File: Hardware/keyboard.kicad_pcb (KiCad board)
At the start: 2 copper layers, 228.8 x 97.4 mm, 57 parts, among them M1 Tab, M10 O, M11 P, M12 Backspace, M13 Esc, M14 A, M15 S, M16 D, M17 F, M18 G, M19 H, M2 Q, M20 J, M21 K, M22 L, M23 ;, M24 ', M25 Shift, M26 Z, M27 X, M28 C, M29 V, M3 W, M30 B, M31 N, M32 M, M33 ,, M34 ., M35 /, M36 Enter, M37 Blnk, M38 Ctrl, M39 Alt, M4 E, M40 Super, M41 Down, M42 Space, M43 Up, M44 L_Ar, M45 D_Ar, M46 U_Ar, M47 R_Ar, M5 R, M6 T, M7 Y, M8 U, M9 I, U1 ROW_1, U2 ROW_2, U3 ROW_3

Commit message: Update
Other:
- outline, holes or cut-outs redrawn
- board text removed: ""Write bussy on it" -Suyash"
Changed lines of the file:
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@@
   (general
     (thickness 1.6)
-    (drawings 7)
+    (drawings 4)
     (tracks 377)
     (zones 0)
@@
     (add_net /SDA_)
     (add_net GND)
-    (add_net "Net-(C1-Pad10)")
-    (add_net "Net-(C1-Pad11)")
-    (add_net "Net-(C1-Pad12)")
-    (add_net "Net-(C1-Pad2)")
-    (add_net "Net-(C1-Pad8)")
-    (add_net "Net-(C1-Pad9)")
-    (add_net "Net-(U1-Pad19)")
-    (add_net "Net-(U2-Pad19)")
-    (add_net "Net-(U2-Pad3)")
-    (add_net "Net-(U3-Pad19)")
   )
   (module Resistor_THT:R_Axial_DIN0204_L3.6mm_D1.6mm_P7.62mm_Horizontal (layer F.Cu)
@@
       (effects (font (size 1 1) (thickness 0.15)))
     )
-    (fp_text user %R (at 3.81 0) (layer F.Fab)
-      (effects (font (size 0.72 0.72) (thickness 0.108)))
-    )
     (fp_line (start 2.01 -0.8) (end 2.01 0.8) (layer F.Fab) (width 0.1))
     (fp_line (start 2.01 0.8) (end 5.61 0.8) (layer F.Fab) (width 0.1))
@@
     (fp_line (start 8.57 1.05) (end 8.57 -1.05) (layer F.CrtYd) (width 0.05))
     (fp_line (start 8.57 -1.05) (end -0.95 -1.05) (layer F.CrtYd) (width 0.05))
+    (fp_text user %R (at 3.81 0) (layer F.Fab)
+      (effects (font (size 0.72 0.72) (thickness 0.108)))
+    )
     (pad 2 thru_hole oval (at 7.62 0 180) (size 1.4 1.4) (drill 0.7) (layers *.Cu *.Mask)
       (net 34 /SCL_))
@@
       (effects (font (size 1 1) (thickness 0.15)))
     )
-    (fp_text user %R (at 3.81 0) (layer F.Fab)
-      (effects (font (size 0.72 0.72) (thickness 0.108)))
-    )
     (fp_line (start 2.01 -0.8) (end 2.01 0.8) (layer F.Fab) (width 0.1))
     (fp_line (start 2.01 0.8) (end 5.61 0.8) (layer F.Fab) (width 0.1))
@@
     (fp_line (start 8.57 1.05) (end 8.57 -1.05) (layer F.CrtYd) (width 0.05))
     (fp_line (start 8.57 -1.05) (end -0.95 -1.05) (layer F.CrtYd) (width 0.05))
+    (fp_text user %R (at 3.81 0) (layer F.Fab)
+      (effects (font (size 0.72 0.72) (thickness 0.108)))
+    )
     (pad 2 thru_hole oval (at 7.62 0 180) (size 1.4 1.4) (drill 0.7) (layers *.Cu *.Mask)
       (net 2 +5V))
@@
   (gr_line (start 101.346 186.182) (end 101.346 88.7476) (layer Edge.Cuts) (width 0.05))
   (gr_line (start 330.1492 186.182) (end 101.346 186.182) (layer Edge.Cuts) (width 0.05))
-  (gr_line (start 101.346 88.7476) (end 327.8632 88.7476) (layer Edge.Cuts) (width 0.05))
-  (gr_line (start 101.346 88.7476) (end 329.9968 88.7476) (layer Edge.Cuts) (width 0.05))
   (gr_line (start 330.1492 88.7476) (end 101.346 88.7476) (layer Edge.Cuts) (width 0.05))
   (gr_line (start 330.1492 186.182) (end 330.1492 88.7476) (layer Edge.Cuts) (width 0.05))
-  (gr_text "\"Write bussy on it\" -Suyash" (at 210.185 146.685) (layer B.SilkS)
-    (effects (font (size 7 7) (thickness 1)) (justify mirror))
-  )
+  (segment (start 293.330908 91.31874) (end 293.72687 91.714702) (width 0.25) (layer F.Cu) (net 0))
   (segment (start 119.47525 108.1564) (end 113.6809 113.95075) (width 0.25) (layer F.Cu) (net 1))
   (segment (start 119.47525 103.345011) (end 119.47525 108.1564) (width 0.25) (layer F.Cu) (net 1))
@@
   (segment (start 251.215901 157.216099) (end 265.132302 171.1325) (width 0.25) (layer F.Cu) (net 33))
   (segment (start 113.325559 91.714702) (end 109.31525 95.725011) (width 0.254) (layer F.Cu) (net 34))
-  (segment (start 293.330908 91.31874) (end 293.72687 91.714702) (width 0.25) (layer F.Cu) (net 0))
   (segment (start 113.325559 91.714702) (end 113.721521 91.31874) (width 0.25) (layer F.Cu) (net 34))
   (segment (start 172.322083 95.725011) (end 176.53 91.517094) (width 0.25) (layer B.Cu) (net 34))

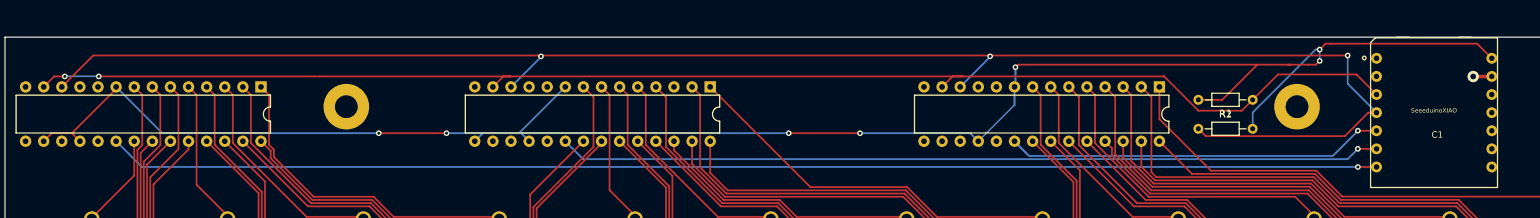
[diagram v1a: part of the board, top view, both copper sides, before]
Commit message: Swapped SDA and SCL pins.
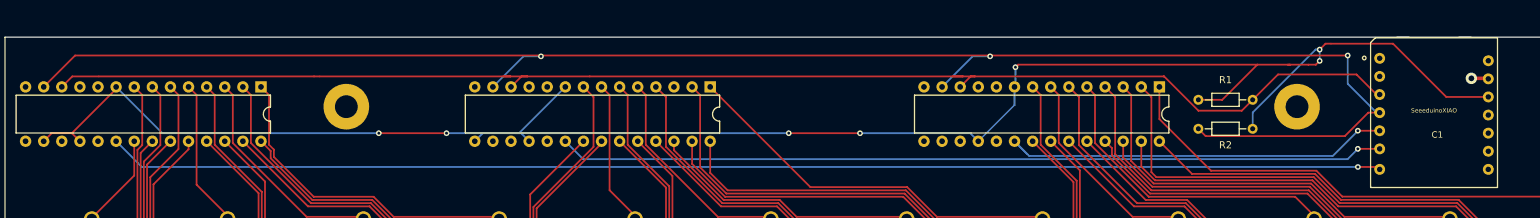
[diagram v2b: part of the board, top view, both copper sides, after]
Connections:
- C1 pad 12: (no net) -> +3V3
- C1 pad 14: +5V -> (no net)
- C1 pad 3: /SDA_ -> /SCL_
- C1 pad 4: /SCL_ -> /SDA_
- R1 pad 1: /SDA_ -> /SCL_
- R1 pad 2: +5V -> +3V3
- R2 pad 1: +5V -> +3V3
- R2 pad 2: /SCL_ -> /SDA_
- U1 pad 18: +5V -> +3V3
- U1 pad 9: +5V -> +3V3
- U2 pad 15: +5V -> +3V3
- U2 pad 18: +5V -> +3V3
- U2 pad 9: +5V -> +3V3
- U3 pad 16: +5V -> +3V3
- U3 pad 18: +5V -> +3V3
- U3 pad 9: +5V -> +3V3
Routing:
- net +3V3: track 0.00 -> 262.9 mm, vias 0 -> 7
- net +5V: track 261.2 -> 0.00 mm, vias 7 -> 0
- net /SDA_: track 199.4 -> 238.4 mm, vias 2 -> 3
- net /SCL_: track 230.7 -> 198.2 mm, vias 3 -> 0
- net (no net): track 0.56 -> 0.00 mm

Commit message: :
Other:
- net class Default removed
